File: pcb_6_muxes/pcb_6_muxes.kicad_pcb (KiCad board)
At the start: 2 copper layers, 167.6 x 48.3 mm, 28 parts, among them U1 74HC4051, U2 74HC4051, U3 74HC4051, U4 74HC4051, U5 74HC4051, U6 74HC4051

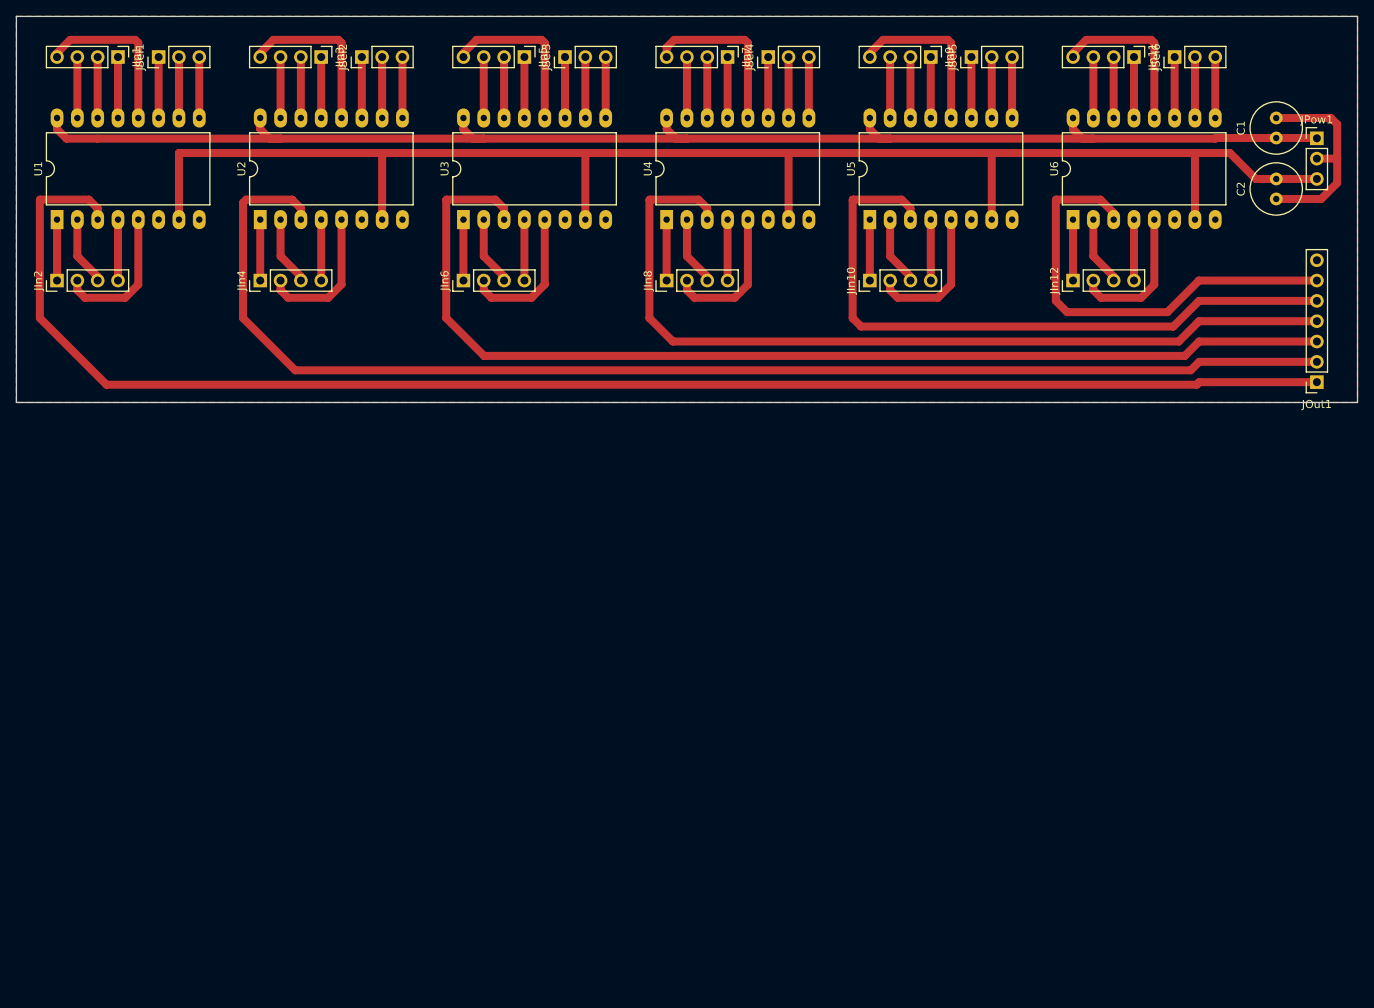
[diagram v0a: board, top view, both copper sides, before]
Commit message: Re-layout with VEE=GND on 121mmx121mm single sided board.
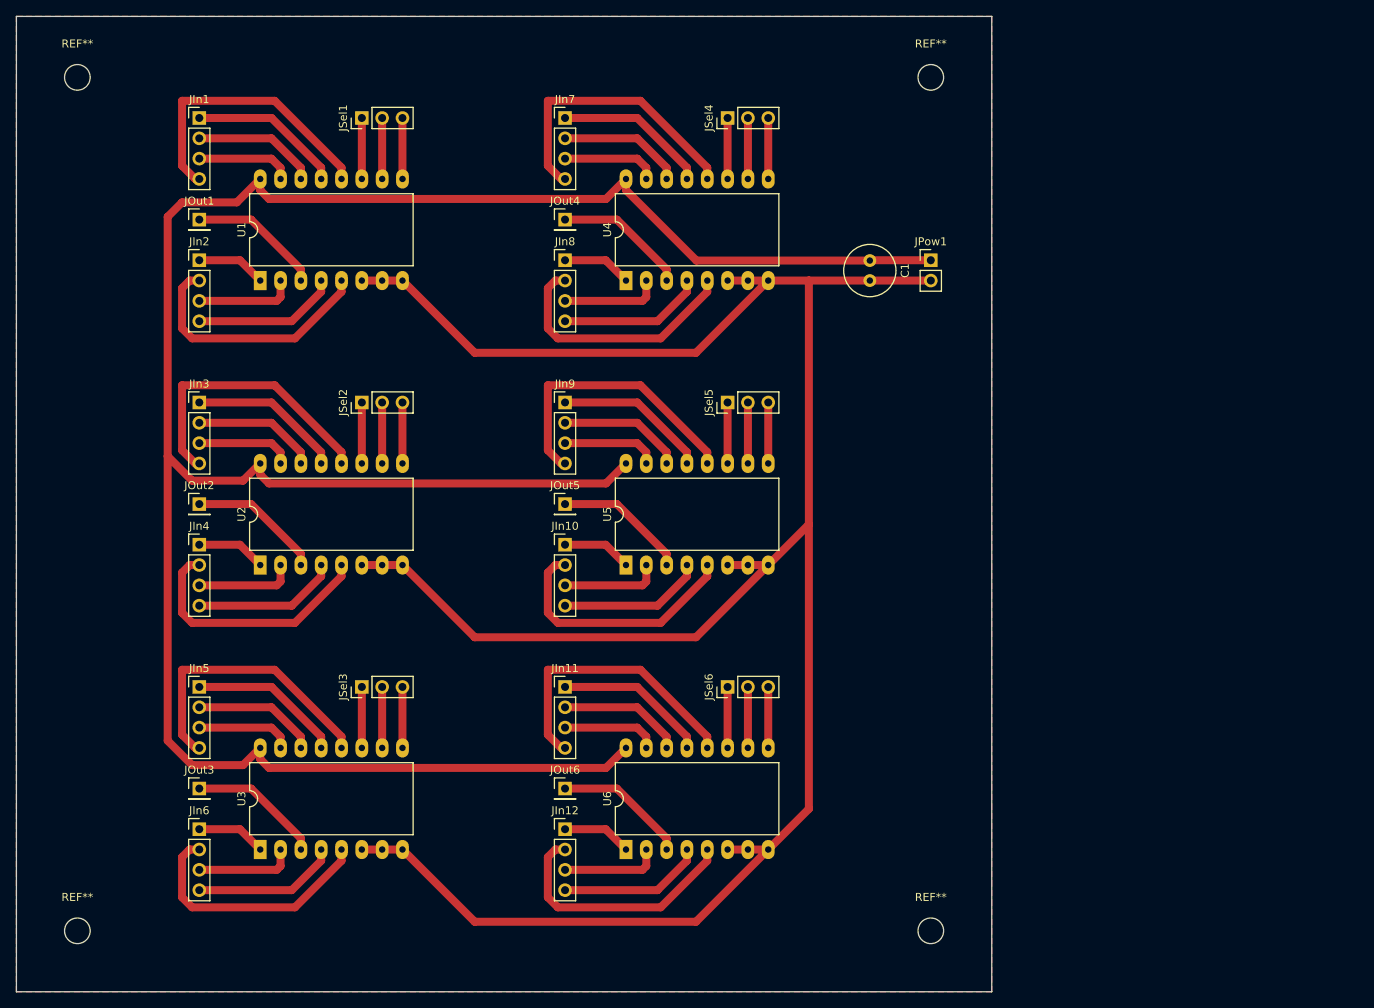
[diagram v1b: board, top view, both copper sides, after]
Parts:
- removed C2: C, Capacitor_THT:C_Radial_D6.3mm_H5.0mm_P2.50mm
- added JOut2: Conn_01x01, Connector_PinHeader_2.54mm:PinHeader_1x01_P2.54mm_Vertical, F.Cu at (88.9, 83.8)
- added JOut3: Conn_01x01, Connector_PinHeader_2.54mm:PinHeader_1x01_P2.54mm_Vertical, F.Cu at (88.9, 119.4)
- added JOut4: Conn_01x01, Connector_PinHeader_2.54mm:PinHeader_1x01_P2.54mm_Vertical, F.Cu at (134.6, 48.3)
- added JOut5: Conn_01x01, Connector_PinHeader_2.54mm:PinHeader_1x01_P2.54mm_Vertical, F.Cu at (134.6, 83.8)
- added JOut6: Conn_01x01, Connector_PinHeader_2.54mm:PinHeader_1x01_P2.54mm_Vertical, F.Cu at (134.6, 119.4)
- added REF**: MountingHole_3.2mm_M3, MountingHole:MountingHole_3.2mm_M3, F.Cu at (180.3, 30.5)
- added REF**: MountingHole_3.2mm_M3, MountingHole:MountingHole_3.2mm_M3, F.Cu at (180.3, 137.2)
- added REF**: MountingHole_3.2mm_M3, MountingHole:MountingHole_3.2mm_M3, F.Cu at (73.7, 137.2)
- added REF**: MountingHole_3.2mm_M3, MountingHole:MountingHole_3.2mm_M3, F.Cu at (73.7, 30.5)
- JOut1: value Conn_01x07 -> Conn_01x01; footprint Connector_PinSocket_2.54mm:PinSocket_1x07_P2.54mm_Vertical -> Connector_PinHeader_2.54mm:PinHeader_1x01_P2.54mm_Vertical
- JPow1: value Conn_01x03 -> Conn_01x02; footprint Connector_PinHeader_2.54mm:PinHeader_1x03_P2.54mm_Vertical -> Connector_PinHeader_2.54mm:PinHeader_1x02_P2.54mm_Vertical
- moved JOut1 141.2 mm to (88.9, 48.3), turned to 0 degrees
- moved JIn11 106.1 mm to (134.6, 106.7), turned to 0 degrees
- moved JSel6 96.6 mm to (154.9, 106.7)
- moved U6 96.6 mm to (142.2, 127.0)
- moved JIn12 93.5 mm to (134.6, 124.5), turned to 0 degrees
- moved JIn5 88.6 mm to (88.9, 106.7), turned to 0 degrees
- moved JSel3 82.7 mm to (109.2, 106.7)
- moved U3 82.7 mm to (96.5, 127.0)
- moved JIn6 76.1 mm to (88.9, 124.5), turned to 0 degrees
- moved JIn9 62.9 mm to (134.6, 71.1), turned to 0 degrees
- moved C1 53.1 mm to (172.7, 53.4), turned to -90 degrees
- moved JSel5 52.9 mm to (154.9, 71.1)
- moved U5 52.9 mm to (142.2, 91.4)
- moved JPow1 50.6 mm to (180.3, 53.3)
- moved JIn10 50.4 mm to (134.6, 88.9), turned to 0 degrees
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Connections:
- net /A0 renamed Net-(JOut1-Pin_1)
- U1 pad 7: VEE -> GND
- U2 pad 3: /A1 -> Net-(JOut2-Pin_1)
- U2 pad 7: VEE -> GND
- U3 pad 3: /A2 -> Net-(JOut3-Pin_1)
- U3 pad 7: VEE -> GND
- U4 pad 3: /A3 -> Net-(JOut4-Pin_1)
- U4 pad 7: VEE -> GND
- U5 pad 3: /A4 -> Net-(JOut5-Pin_1)
- U5 pad 7: VEE -> GND
- U6 pad 3: /A5 -> Net-(JOut6-Pin_1)
- U6 pad 7: VEE -> GND
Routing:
- net GND: track 26.3 -> 290.8 mm
- net VEE: track 193.5 -> 0.00 mm
- net Net-(JOut1-Pin_1): track 187.1 -> 16.7 mm
- net /A1: track 161.0 -> 0.00 mm
- net /A2: track 135.4 -> 0.00 mm
- net VCC: track 181.6 -> 295.5 mm
- net /A3: track 109.6 -> 0.00 mm
- net /A4: track 83.7 -> 0.00 mm
- net /A5: track 56.2 -> 0.00 mm
- net Net-(JOut6-Pin_1): track 0.00 -> 16.7 mm
- net Net-(JOut4-Pin_1): track 0.00 -> 16.7 mm
- net Net-(JOut3-Pin_1): track 0.00 -> 16.7 mm
- net Net-(JOut5-Pin_1): track 0.00 -> 16.7 mm
- net Net-(JOut2-Pin_1): track 0.00 -> 16.7 mm
- net Net-(JIn1-Pin_4): track 20.9 -> 35.8 mm
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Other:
- board size 167.6 x 48.3 mm -> 121.9 x 121.9 mm
